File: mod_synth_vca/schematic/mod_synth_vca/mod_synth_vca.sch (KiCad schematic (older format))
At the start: 11 parts

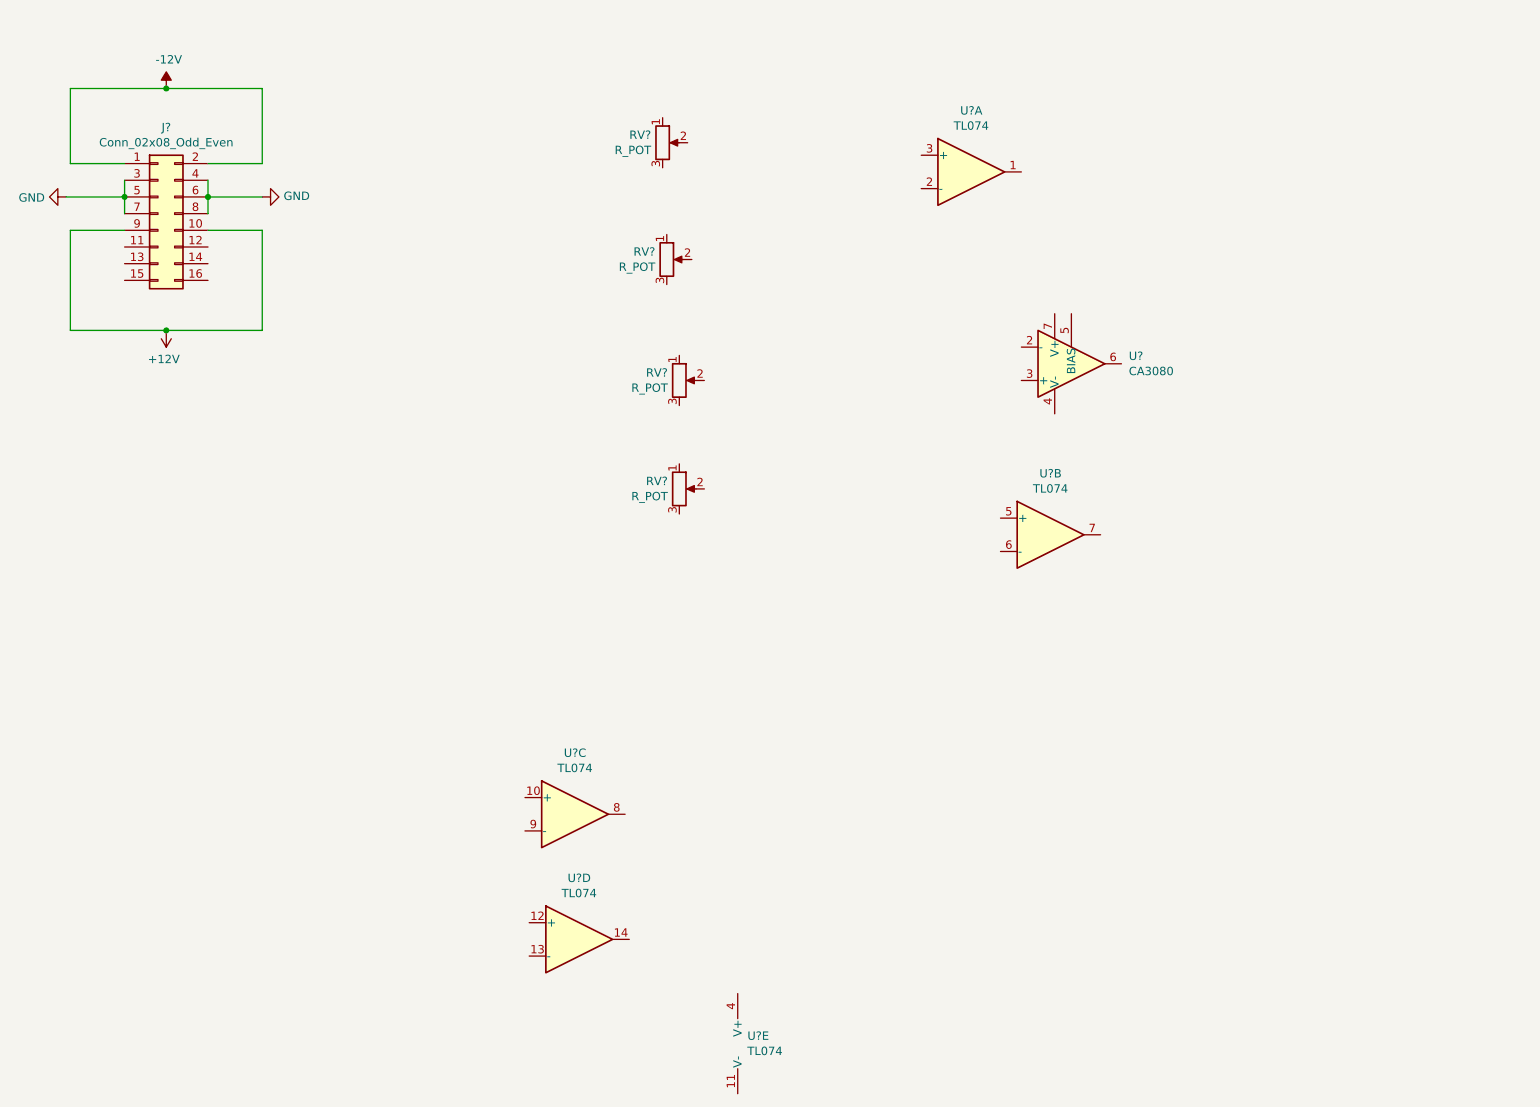
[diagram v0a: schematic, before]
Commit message: Add more components to schematic
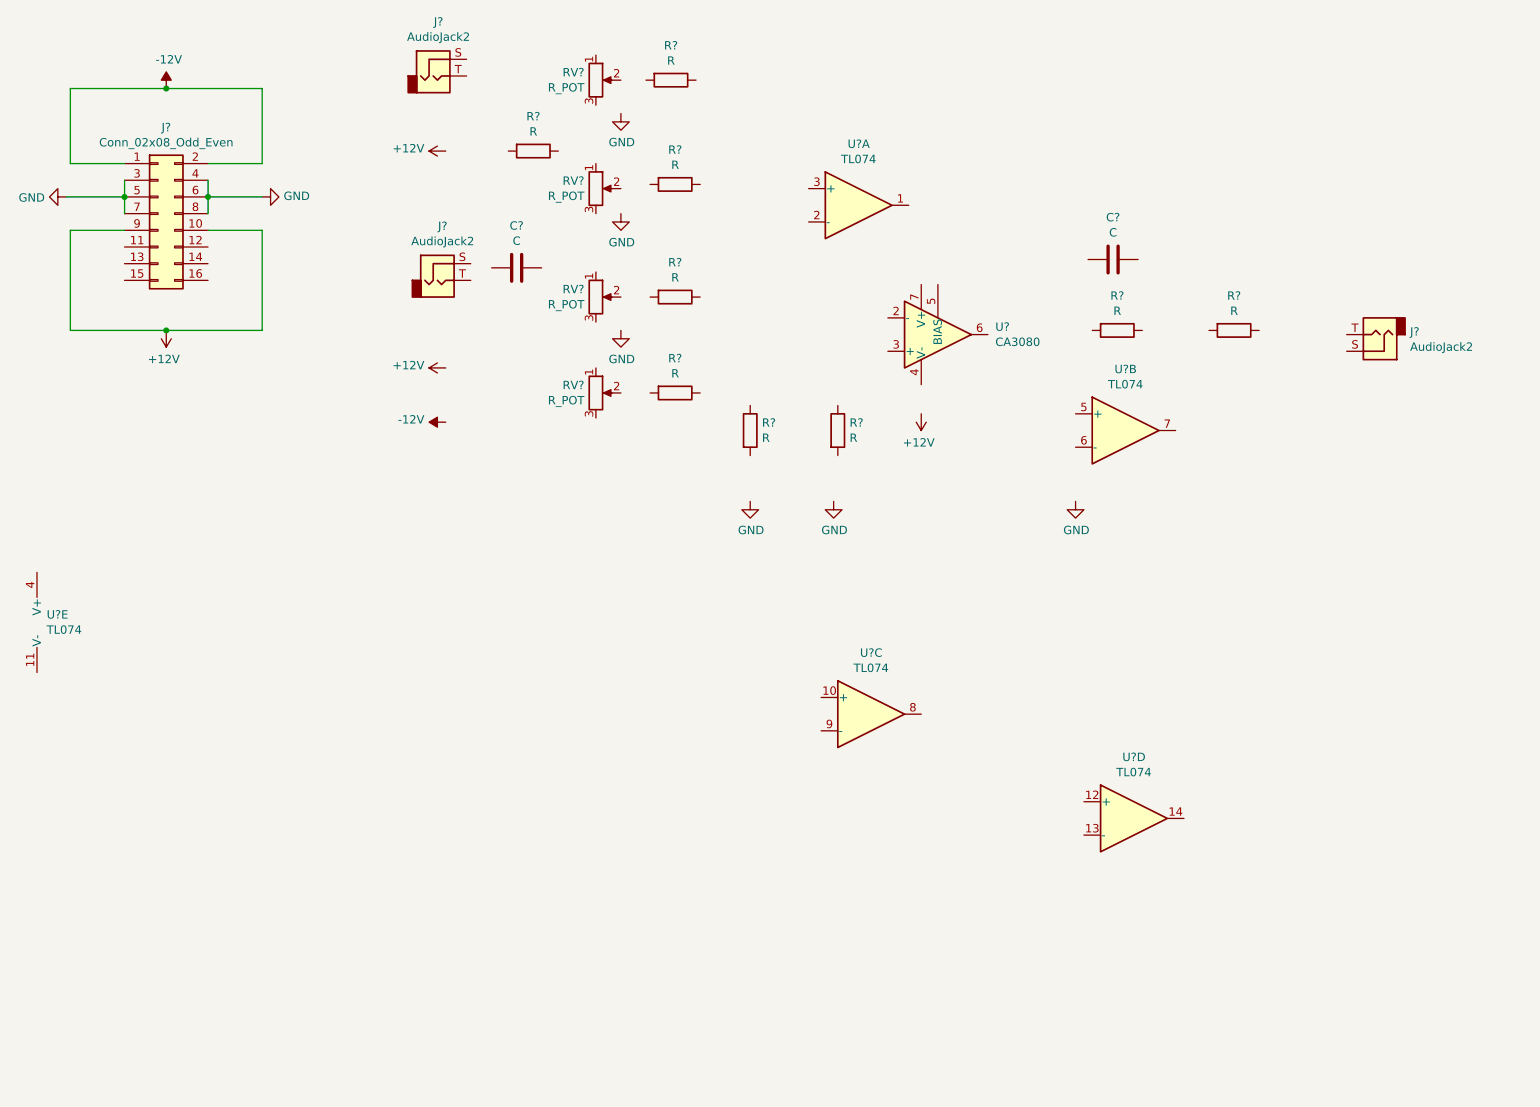
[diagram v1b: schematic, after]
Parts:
- added C? (x2): C, symbol Device:C
- added J? (x3): AudioJack2, symbol Connector:AudioJack2
- added R? (x9): R, symbol Device:R
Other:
- moved on the sheet: RV?, U?, U?A, U?B, U?C, U?D, U?E

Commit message: Complete schematic for single input vca
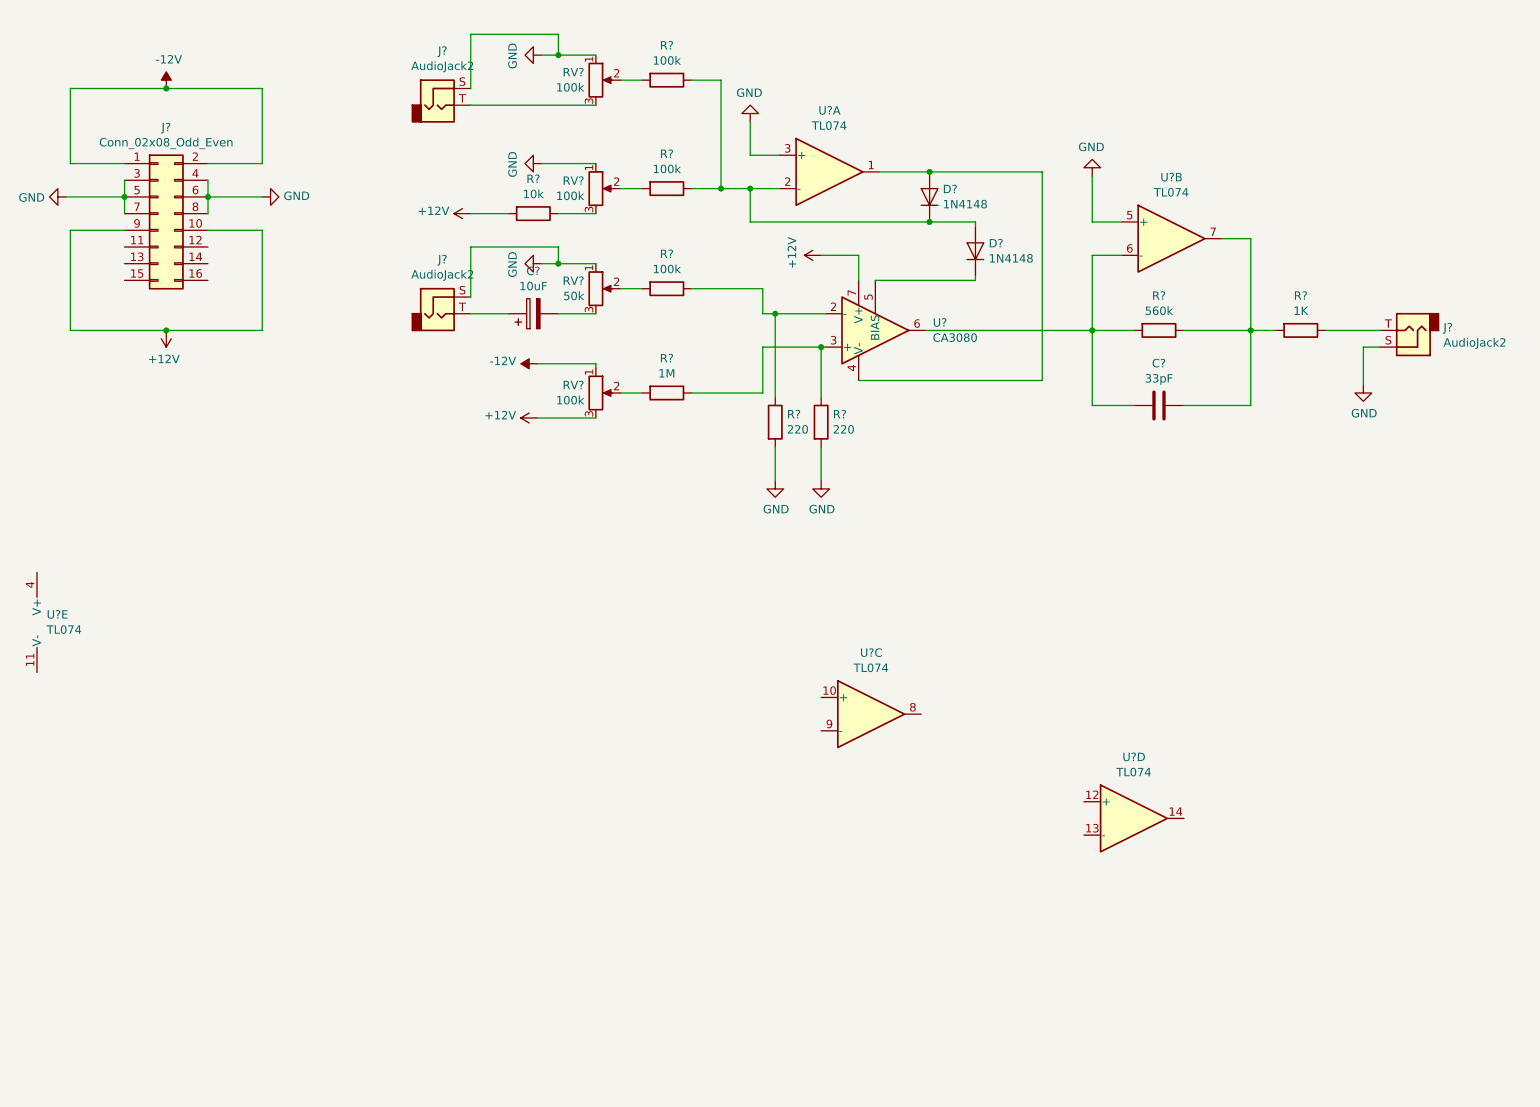
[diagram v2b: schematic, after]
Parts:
- removed C?: C, symbol Device:C
- added C?: 10uF, symbol Device:CP
- added D? (x2): 1N4148, symbol Device:D
- C?: value C -> 33pF
- R? (x3): value R -> 100k
- R?: value R -> 10k
- R?: value R -> 1M
- R? (x2): value R -> 220
- R?: value R -> 560k
- R?: value R -> 1K
- RV? (x3): value R_POT -> 100k
- RV?: value R_POT -> 50k
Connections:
- net +12V: now also R?.2, RV?.3, U?.7 (V+)
- net -12V: now also RV?.1
- net GND: now also J?.S, J?.S, J?.S, R?.2, R?.2, RV?.1, RV?.1, RV?.1, U?.3 (+), U?.5 (+)
- net at U?.2 (-): now also R?.1, R?.1
- net at U?.3 (+): now also R?.1, R?.1
- net at U?.4 (V-): now also U?.1, D?.2 (A)
- net at U?.5 (BIAS): now also D?.1 (K)
- net at U?.6: now also C?.2, R?.2, U?.6 (-)
- net at R?.1: now also R?.1, U?.2 (-), D?.1 (K), D?.2 (A)
- net at R?.2: now also RV?.2 (x4)
- net at R?.1: now also RV?.3
- net at U?.7: now also C?.1, R?.1, R?.2
- net at RV?.3: now also J?.T
- net at R?.1: now also J?.T
- net at RV?.3: now also C?.2
- net at J?.T: now also C?.1
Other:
- moved on the sheet: C?, J?, R?, RV?, U?, U?A, U?B
